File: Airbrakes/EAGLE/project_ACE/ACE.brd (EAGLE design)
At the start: 99.7 x 61 mm, 15 parts, among them J3 PTH

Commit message: ACE PCB updates
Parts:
- removed PAD1, PAD2: (no value), wirepad:2,15/1,0
- removed R1, R2: 0 ohm, fab_new:R1206
- added ROTARY_TERMINAL: CONN_02_TERM-ADAFRUIT, fab_new:3.5MMTERM
- moved 0OHM 1.27 mm to (90.6, 52.3)
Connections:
- removed net N$2: R1.2, R2.1
- net GND: now also ROTARY_TERMINAL.1, ROTARY_TERMINAL.2; no longer PAD1.1, PAD2.1, R2.2
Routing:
- net GND: track 195.2 -> 243.9 mm
- net SCL: track 123.9 -> 126.9 mm
- net SDA: track 117.6 -> 119.1 mm
- net N$3: track 1.27 -> 0.00 mm
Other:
- board text removed: "rotary_switch"

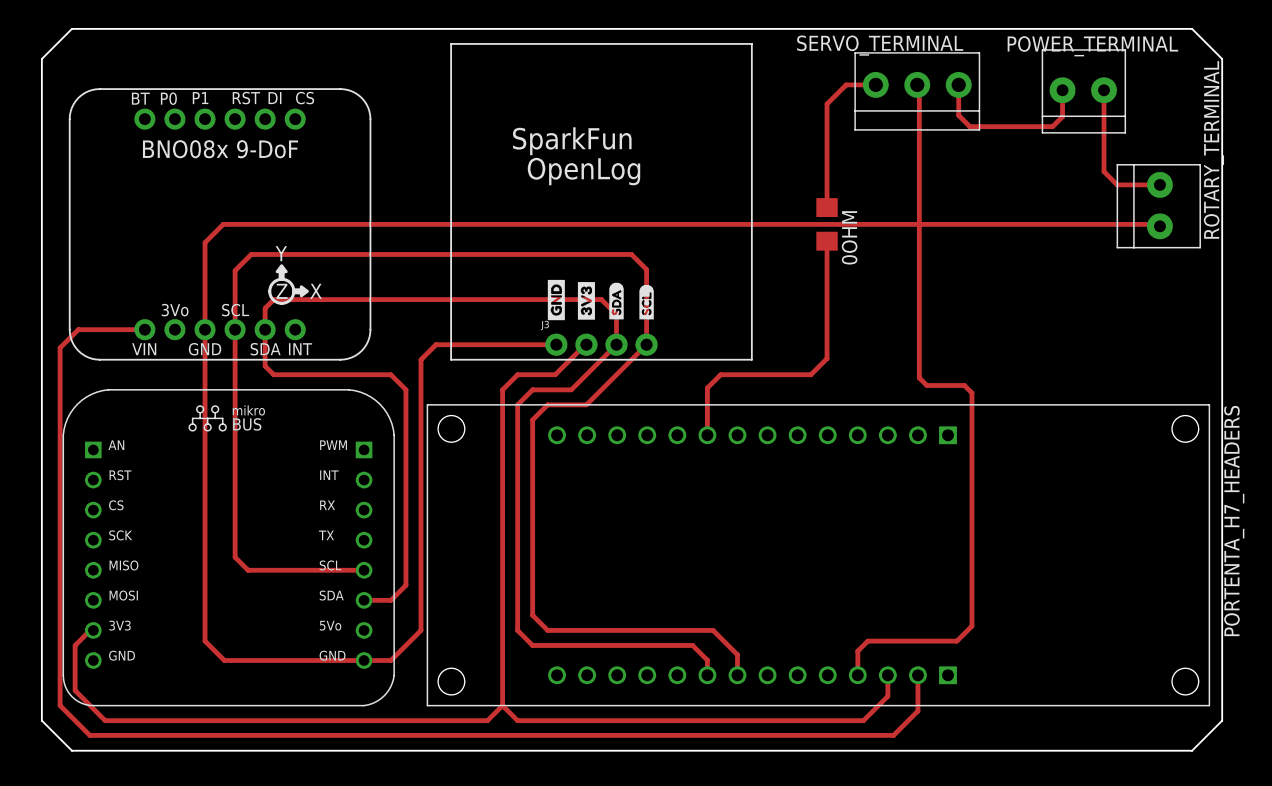
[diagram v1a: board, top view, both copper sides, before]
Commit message: Resize to 100mmx62mm
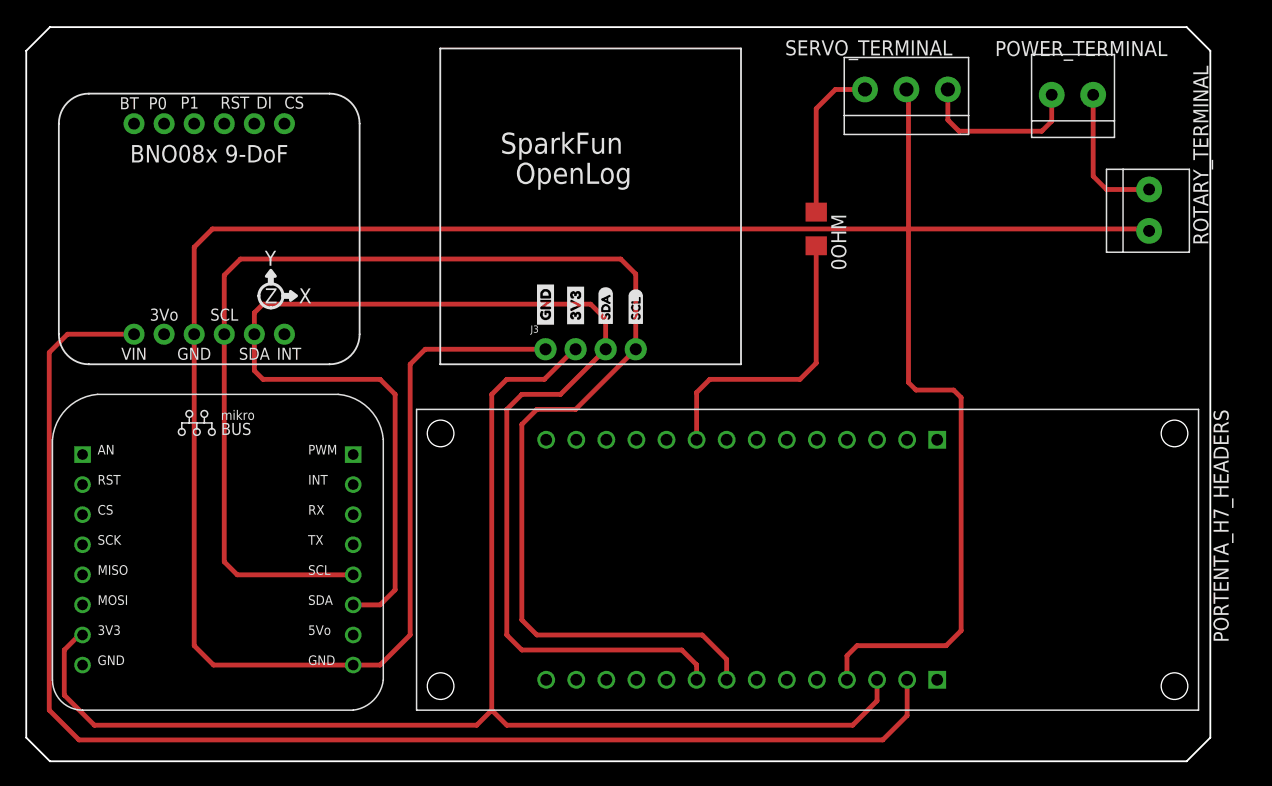
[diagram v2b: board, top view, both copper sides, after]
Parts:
- moved ROTARY_TERMINAL 0.99 mm to (117.8, 53.6)
- moved U$10 0.99 mm to (89.0, 24.0)
- moved U$1 0.99 mm to (25.2, 10.0)
- moved SERVO_TERMINAL 0.99 mm to (97.3, 63.7)
- moved 0OHM 0.99 mm to (89.7, 52.0)
- moved J3 0.99 mm to (66.9, 41.8)
- moved POWER_TERMINAL 0.99 mm to (111.3, 63.3)
- moved U$16 0.99 mm to (71.9, 43.6)
- moved U$19 0.99 mm to (74.5, 43.6)
- moved U$5 0.99 mm to (24.5, 39.3)
- moved U$8 0.99 mm to (69.4, 43.4)
- moved U$9 0.99 mm to (66.9, 43.4)
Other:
- board size 99.7 x 61 mm -> 100 x 62 mm

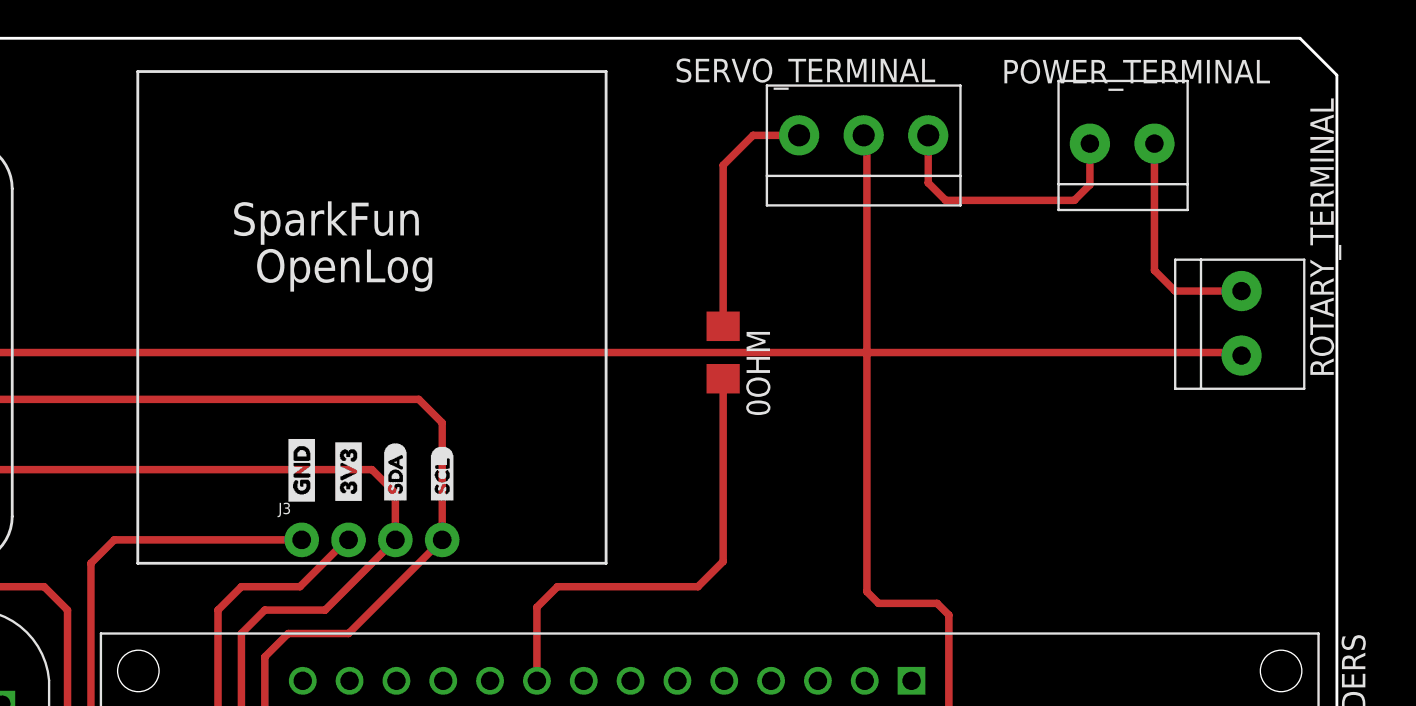
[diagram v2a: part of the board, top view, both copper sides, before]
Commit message: change terminals on ACE PCB to 200mil pitch
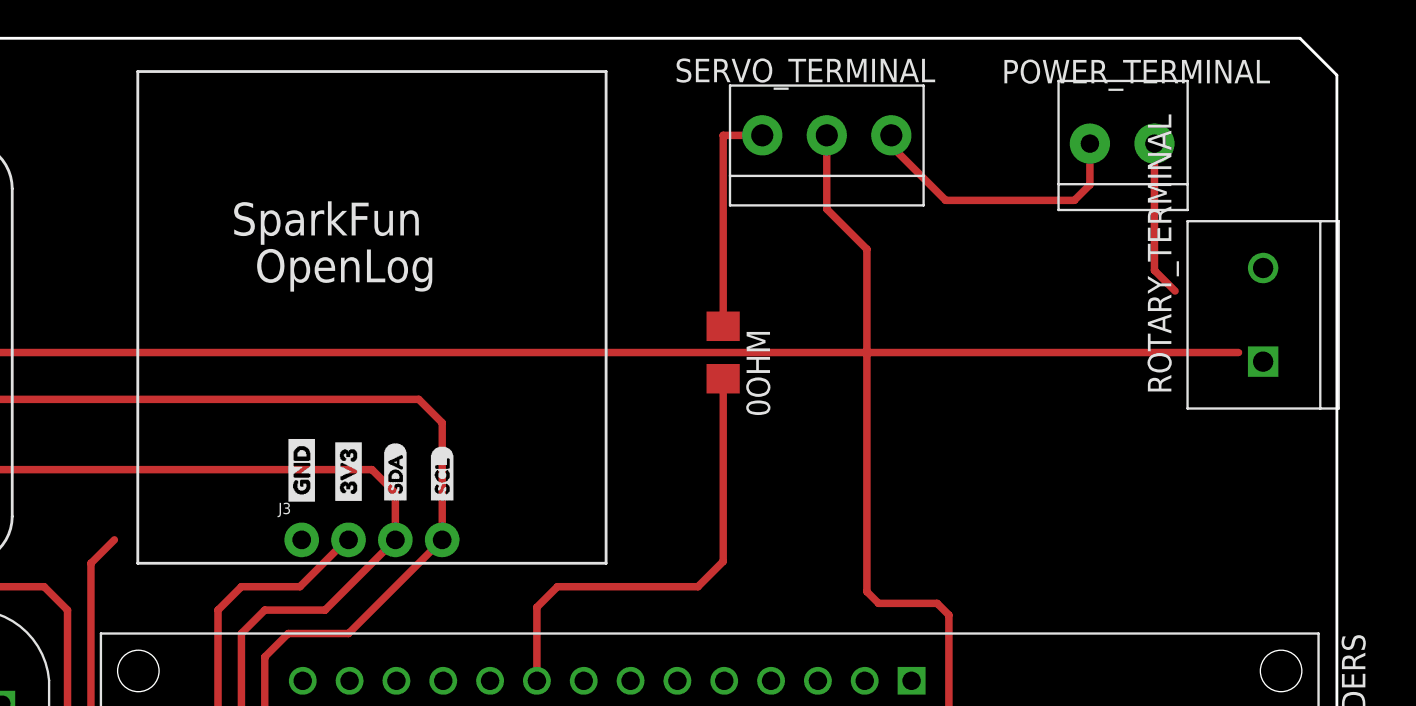
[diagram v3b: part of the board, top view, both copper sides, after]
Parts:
- ROTARY_TERMINAL: value CONN_02_TERM-ADAFRUIT -> 282837-2; device fab_new:3.5MMTERM -> 282837-2:TE_282837-2
- moved SERVO_TERMINAL 2.00 mm to (95.3, 63.7)
- moved ROTARY_TERMINAL 1.24 mm to (119.0, 54.0), turned to 90 degrees
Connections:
- new net N$2: J3.1, ROTARY_TERMINAL.1, ROTARY_TERMINAL.2
- net GND: no longer J3.1, ROTARY_TERMINAL.1, ROTARY_TERMINAL.2
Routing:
- net GND: track 243.9 -> 230.7 mm
- net PWM: track 38.6 -> 37.5 mm
- net 7.4V: track 14.3 -> 15.2 mm
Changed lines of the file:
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@@
 <attribute name="NAME" x="104.814" y="66.556" size="1.27" layer="25"/>
 </element>
-<element name="SERVO_TERMINAL" library="fab_new" package="ED555DS-3DS" value="CONN_03_TERM'-FABLAB'" x="97.334" y="63.736" smashed="yes"/>
+<element name="SERVO_TERMINAL" library="fab_new" package="ED555DS-3DS" value="CONN_03_TERM'-FABLAB'" x="95.334" y="63.736" smashed="yes"/>
 <element name="0OHM" library="fab_new" package="R1206" value="" x="89.714" y="51.956" smashed="yes" rot="R270">
 <attribute name="NAME" x="90.984" y="53.226" size="1.27" layer="25" rot="R270"/>
@@
 </element>
 <element name="U$1" library="MIKROE-4903" package="MIKROE-ALTITUDE-6-CLICK-PINOUT" value="MIKROE-ALTITUDE-6-CLICK-DVC" x="25.214" y="10.046" smashed="yes"/>
-<element name="ROTARY_TERMINAL" library="fab_new" package="3.5MMTERM" value="CONN_02_TERM-ADAFRUIT" x="117.829" y="53.591" smashed="yes" rot="R270">
-<attribute name="NAME" x="122.829" y="50.591" size="1.27" layer="25" rot="R90"/>
+<element name="ROTARY_TERMINAL" library="282837-2" package="TE_282837-2" value="282837-2" x="119" y="54" smashed="yes" rot="R90">
+<attribute name="AVAILABILITY" value="In Stock" x="119" y="54" size="1.778" layer="27" rot="R90" display="off"/>
+<attribute name="CHECK_PRICES" value="https://www.snapeda.com/parts/282837-2/TE+Connectivity+AMP+Connectors/view-part/?ref=eda" x="119" y="54" size="1.778" layer="27" rot="R90" display="off"/>
+<attribute name="COMMENT" value="282837-2" x="119" y="54" size="1.778" layer="27" rot="R90" display="off"/>
+<attribute name="DESCRIPTION" value=" Terminal Block Connector Wire Receptacle 2 5.08 mm 30-16 AWG Green 13.5 A 250 V | TE Connectivity 282837-2 " x="119" y="54" size="1.778" layer="27" rot="R90" display="off"/>
+<attribute name="MF" value="TE Connectivity" x="119" y="54" size="1.778" layer="27" rot="R90" display="off"/>
+<attribute name="MP" value="282837-2" x="119" y="54" size="1.778" layer="27" rot="R90" display="off"/>
+<attribute name="NAME" x="114.02135" y="49.69126875" size="1.272590625" layer="25" rot="R90"/>
+<attribute name="PACKAGE" value="None" x="119" y="54" size="1.778" layer="27" rot="R90" display="off"/>
+<attribute name="PRICE" value="None" x="119" y="54" size="1.778" layer="27" rot="R90" display="off"/>
+<attribute name="PURCHASE-URL" value="https://www.snapeda.com/api/url_track_click_mouser/?unipart_id=2549980&amp;manufacturer=TE Connectivity&amp;part_name=282837-2&amp;search_term=None" x="119" y="54" size="1.778" layer="27" rot="R90" display="off"/>
+<attribute name="SNAPEDA_LINK" value="https://www.snapeda.com/parts/282837-2/TE+Connectivity+AMP+Connectors/view-part/?ref=snap" x="119" y="54" size="1.778" layer="27" rot="R90" display="off"/>
+<attribute name="VALUE" x="125.484090625" y="49.688759375" size="1.27331875" layer="27" rot="R90"/>
 </element>
 </elements>
 <signals>
 <signal name="GND" class="2">
-<contactref element="J3" pad="1"/>
 <contactref element="U$5" pad="GND"/>
 <contactref element="U$10" pad="J18"/>
-<wire x1="66.854" y1="41.796" x2="56.694" y2="41.796" width="0.4064" layer="1"/>
 <wire x1="92.3114" y1="13.8814" x2="92.3114" y2="15.9134" width="0.4064" layer="1"/>
 <contactref element="POWER_TERMINAL" pad="1"/>
@@
 <wire x1="37.184" y1="16.761" x2="38.819" y2="15.126" width="0.4064" layer="1"/>
 <wire x1="37.184" y1="43.066" x2="37.184" y2="50.416" width="0.4064" layer="1"/>
-<contactref element="ROTARY_TERMINAL" pad="2"/>
-<contactref element="ROTARY_TERMINAL" pad="1"/>
 <wire x1="113.104" y1="63.286" x2="113.104" y2="56.411" width="0.4064" layer="1"/>
-<wire x1="114.224" y1="55.291" x2="117.829" y2="55.291" width="0.4064" layer="1"/>
 <wire x1="113.104" y1="56.411" x2="114.224" y2="55.291" width="0.4064" layer="1"/>
 <wire x1="93.159" y1="16.761" x2="100.684" y2="16.761" width="0.4064" layer="1"/>
 <wire x1="100.684" y1="16.761" x2="101.954" y2="18.031" width="0.4064" layer="1"/>
 <wire x1="92.3114" y1="15.9134" x2="93.159" y2="16.761" width="0.4064" layer="1"/>
-<wire x1="117.829" y1="51.791" x2="117.664" y2="51.956" width="0.4064" layer="1"/>
 <wire x1="37.184" y1="50.416" x2="38.724" y2="51.956" width="0.4064" layer="1"/>
 <wire x1="38.724" y1="51.956" x2="117.664" y2="51.956" width="0.4064" layer="1"/>
-<wire x1="97.509" y1="63.561" x2="97.334" y2="63.736" width="0.4064" layer="1"/>
+<wire x1="97.509" y1="57.561" x2="95.334" y2="59.736" width="0.4064" layer="1"/>
+<wire x1="95.334" y1="59.736" x2="95.334" y2="63.736" width="0.4064" layer="1"/>
 <wire x1="101.954" y1="18.031" x2="101.954" y2="37.716" width="0.4064" layer="1"/>
 <wire x1="101.954" y1="37.716" x2="101.319" y2="38.351" width="0.4064" layer="1"/>
 <wire x1="101.319" y1="38.351" x2="98.144" y2="38.351" width="0.4064" layer="1"/>
 <wire x1="98.144" y1="38.351" x2="97.509" y2="38.986" width="0.4064" layer="1"/>
-<wire x1="97.509" y1="38.986" x2="97.509" y2="63.561" width="0.4064" layer="1"/>
-<wire x1="117.829" y1="51.791" x2="117.829" y2="55.291" width="0" layer="19" extent="1-1"/>
-<wire x1="97.334" y1="63.736" x2="113.104" y2="63.286" width="0" layer="19" extent="1-1"/>
+<wire x1="97.509" y1="38.986" x2="97.509" y2="57.561" width="0.4064" layer="1"/>
+<wire x1="117.664" y1="51.956" x2="114.224" y2="55.291" width="0" layer="19" extent="1-1"/>
+<wire x1="95.334" y1="63.736" x2="113.104" y2="63.286" width="0" layer="19" extent="1-1"/>
 </signal>
 <signal name="VCC" class="2">
@@
 <wire x1="109.604" y1="63.286" x2="109.604" y2="61.051" width="0.4064" layer="1"/>
 <wire x1="109.604" y1="61.051" x2="108.764" y2="60.211" width="0.4064" layer="1"/>
-<wire x1="101.779" y1="60.211" x2="100.834" y2="61.156" width="0.4064" layer="1"/>
-<wire x1="100.834" y1="61.156" x2="100.834" y2="63.736" width="0.4064" layer="1"/>
+<wire x1="101.779" y1="60.211" x2="98.834" y2="63.156" width="0.4064" layer="1"/>
+<wire x1="98.834" y1="63.156" x2="98.834" y2="63.736" width="0.4064" layer="1"/>
 <wire x1="108.764" y1="60.211" x2="101.779" y2="60.211" width="0.4064" layer="1"/>
 </signal>
@@
 <contactref element="0OHM" pad="1"/>
 <contactref element="SERVO_TERMINAL" pad="1"/>
-<wire x1="89.714" y1="53.378" x2="89.714" y2="62.116" width="0.4064" layer="1"/>
-<wire x1="91.334" y1="63.736" x2="93.834" y2="63.736" width="0.4064" layer="1"/>
-<wire x1="89.714" y1="62.116" x2="91.334" y2="63.736" width="0.4064" layer="1"/>
+<wire x1="89.714" y1="53.378" x2="89.714" y2="63.736" width="0.4064" layer="1"/>
+<wire x1="89.714" y1="63.736" x2="91.834" y2="63.736" width="0.4064" layer="1"/>
 <contactref element="U$10" pad="J9"/>
 <contactref element="0OHM" pad="2"/>
@@
 <contactref element="U$1" pad="GND_0"/>
 </signal>
+<signal name="N$2" class="2">
+<contactref element="J3" pad="1"/>
+<contactref element="ROTARY_TERMINAL" pad="1"/>
+<contactref element="ROTARY_TERMINAL" pad="2"/>
+<wire x1="119" y1="56.54" x2="66.854" y2="41.796" width="0" layer="19" extent="1-1"/>
+<wire x1="119" y1="51.46" x2="119" y2="56.54" width="0" layer="19" extent="1-1"/>
+</signal>
 </signals>
